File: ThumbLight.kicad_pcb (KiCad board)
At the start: 2 copper layers, 33 x 49 mm, 12 parts, among them J1 USB_A, SW1 RESET, SW2 A, SW3 B, SW4 MODE, U1 DHT11, U2 UA78M33_TO252, U3 ESP-12E, U4 TTL

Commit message: v1.1-beta improvements
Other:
- board text added: "TODO: - Regulator needs more space - Neopixel needs more space and flat underground"
- board text added: "v1.1-beta"
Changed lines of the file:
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@@
     (pad_to_mask_clearance 0)
     (pcbplotparams
-      (layerselection 0x0001000_fffffffe)
+      (layerselection 0x0000000_fffffffe)
       (disableapertmacros false)
       (usegerberextensions false)
@@
       (hpglpendiameter 15.000000)
       (dxfpolygonmode true)
-      (dxfimperialunits true)
+      (dxfimperialunits false)
       (dxfusepcbnewfont true)
       (psnegative false)
@@
     (effects (font (size 1.5 1.5) (thickness 0.3)))
   )
+  (gr_text "v1.1-beta" (at 101 97 90) (layer "F.SilkS")
+    (effects (font (size 1.5 1.5) (thickness 0.3)))
+  )
+  (gr_text "TODO:\n\n- Regulator needs more space\n- Neopixel needs more space and flat underground\n" (at 95 51) (layer "F.Fab")
+    (effects (font (size 1.5 1.5) (thickness 0.3)) (justify left))
+  )
   (segment (start 84 116.971493) (end 84 113.075) (width 0.6) (layer "B.Cu") (net 1))

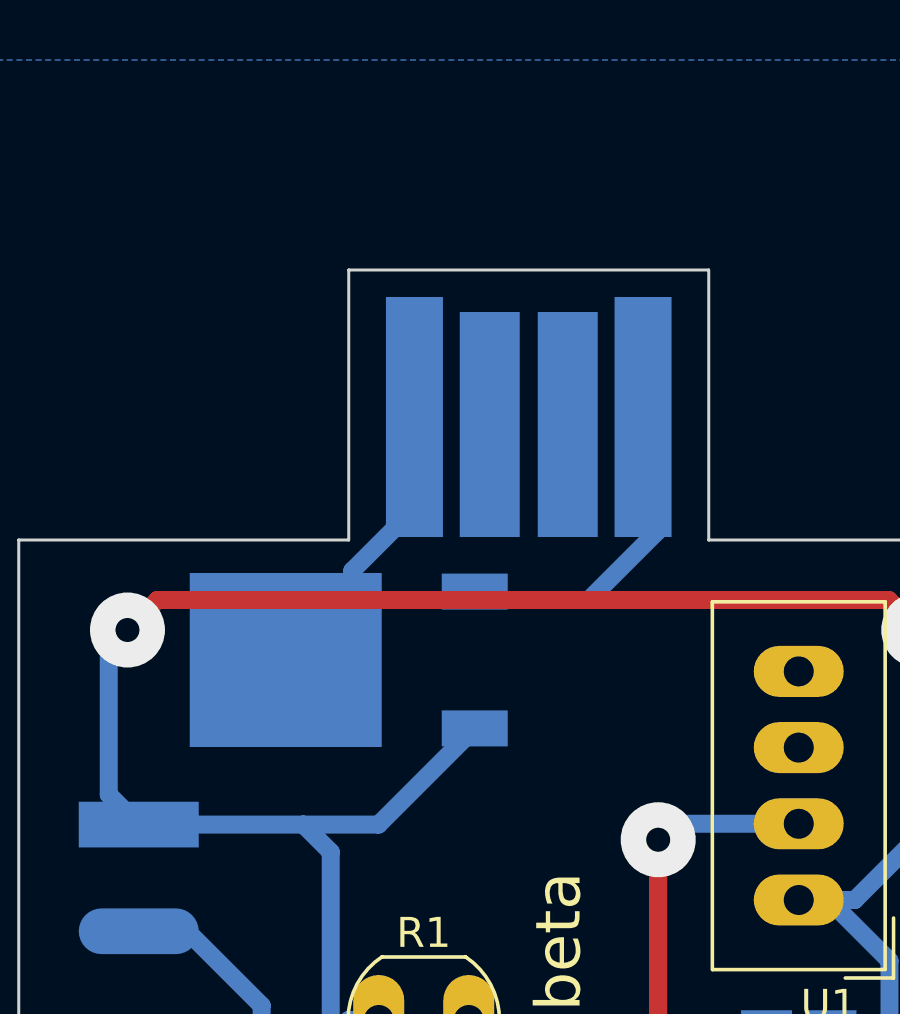
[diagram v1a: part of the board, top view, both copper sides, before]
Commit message: Elongate USB Plug
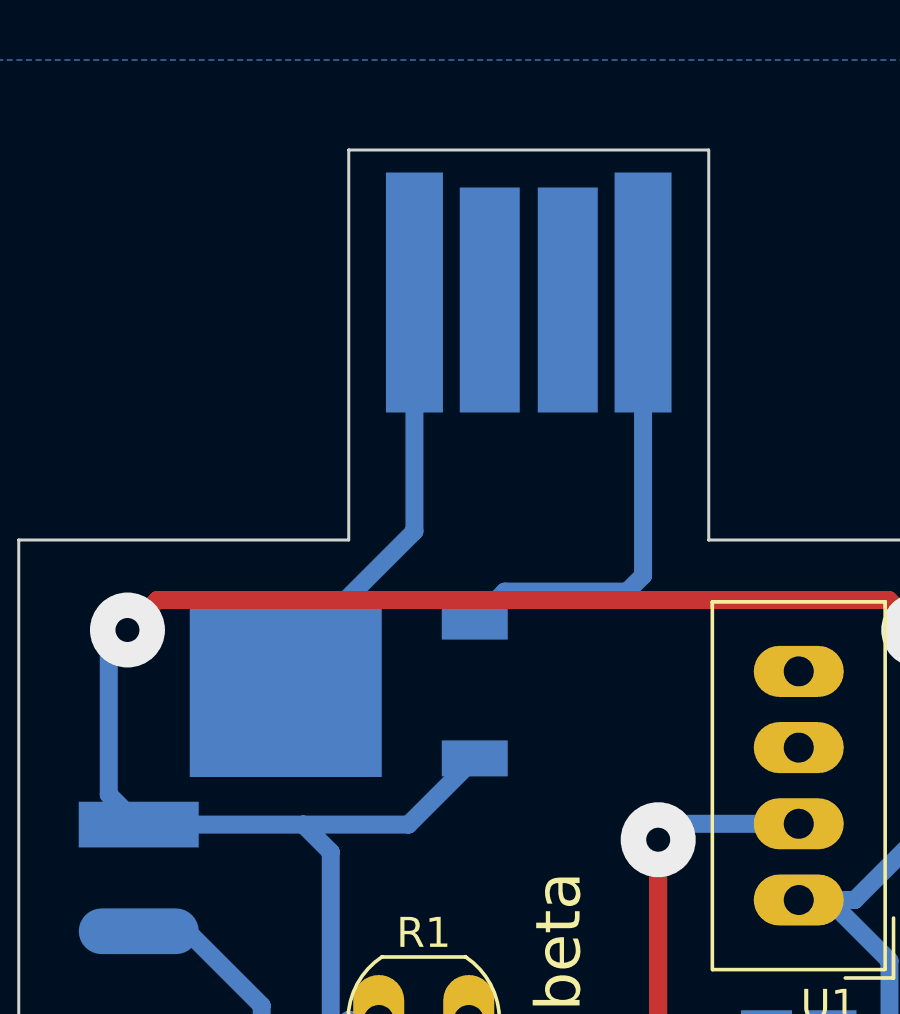
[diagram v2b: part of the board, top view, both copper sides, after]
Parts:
- moved J1 4.15 mm to (100.0, 67.8)
- moved U2 1.00 mm to (94.0, 86.0)
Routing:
- net GND: track 33.9 -> 39.1 mm
- net +5V: track 11.2 -> 15.7 mm
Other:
- board size 33 x 49 mm -> 33 x 53 mm
- board text added: "TODO: - Regulator needs more space - Neopixel needs more space and flat underground - Switches pads need to move to the outside of the switch"
- board text removed: "TODO: - Regulator needs more space - Neopixel needs more space and flat underground"
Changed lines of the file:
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@@
   )
   (footprint "usb-a-pcb:usb-a-pcb" (layer "B.Cu")
-    (at 100 72 180)
+    (at 100 67.85 180)
     (property "Sheetfile" "ThumbLight.kicad_sch")
     (property "Sheetname" "")
@@
       (polygon
         (pts
-          (xy 94 82)
-          (xy 106 82)
-          (xy 106 72)
-          (xy 94 72)
+          (xy 94 77.85)
+          (xy 106 77.85)
+          (xy 106 67.85)
+          (xy 94 67.85)
         )
       )
@@
   )
   (footprint "Package_TO_SOT_SMD:TO-252-2" (layer "B.Cu")
-    (at 94 85 180)
+    (at 94 86 180)
     (descr "TO-252 / DPAK SMD package, http://www.infineon.com/cms/en/product/packages/PG-TO252/PG-TO252-3-1/")
     (tags "DPAK TO-252 DPAK-3 TO-252-3 SOT-428")
@@
       (xy 83 81)
       (xy 94 81)
-      (xy 94 72)
-      (xy 106 72)
+      (xy 94 68)
+      (xy 106 68)
     ) (layer "Edge.Cuts") (width 0.1) (fill none))
   (gr_line (start 100 71) (end 100 129) (layer "F.Fab") (width 0.1))
@@
     (effects (font (size 1.5 1.5) (thickness 0.3)))
   )
-  (gr_text "TODO:\n\n- Regulator needs more space\n- Neopixel needs more space and flat underground\n" (at 95 51) (layer "F.Fab")
+  (gr_text "TODO:\n\n- Regulator needs more space\n- Neopixel needs more space and flat underground\n- Switches pads need to move to the outside of the switch" (at 95 51) (layer "F.Fab")
     (effects (font (size 1.5 1.5) (thickness 0.3)) (justify left))
   )
   (segment (start 84 116.971493) (end 84 113.075) (width 0.6) (layer "B.Cu") (net 1))
   (segment (start 84 108.925) (end 84 113.075) (width 0.6) (layer "B.Cu") (net 1))
+  (segment (start 91.9 85) (end 91.9 86) (width 0.6) (layer "B.Cu") (net 1))
   (segment (start 84.501497 117.47299) (end 84 116.971493) (width 0.6) (layer "B.Cu") (net 1))
-  (segment (start 94.12 82.02) (end 94.12 82.78) (width 0.6) (layer "B.Cu") (net 1))
-  (segment (start 94.12 82.78) (end 91.9 85) (width 0.6) (layer "B.Cu") (net 1))
   (segment (start 84 101.925) (end 84 113.075) (width 0.6) (layer "B.Cu") (net 1))
-  (segment (start 96.19 79.95) (end 94.12 82.02) (width 0.6) (layer "B.Cu") (net 1))
+  (segment (start 96.19 80.71) (end 91.9 85) (width 0.6) (layer "B.Cu") (net 1))
   (segment (start 88.651497 117.47299) (end 84.501497 117.47299) (width 0.6) (layer "B.Cu") (net 1))
-  (segment (start 96.19 76.9) (end 96.19 79.95) (width 0.6) (layer "B.Cu") (net 1))
+  (segment (start 96.19 72.75) (end 96.19 80.71) (width 0.6) (layer "B.Cu") (net 1))
   (segment (start 113 84) (end 112 83) (width 0.6) (layer "F.Cu") (net 2))
   (segment (start 87.624255 83) (end 86.624255 84) (width 0.6) (layer "F.Cu") (net 2))
@@
   (segment (start 112.025 112.022535) (end 112.317294 112.314829) (width 0.6) (layer "B.Cu") (net 2))
   (segment (start 93.399501 91.399501) (end 92.48618 90.48618) (width 0.6) (layer "B.Cu") (net 2))
+  (segment (start 95.99382 90.48618) (end 98.2 88.28) (width 0.6) (layer "B.Cu") (net 2))
   (segment (start 96 114.100499) (end 94.600499 115.5) (width 0.6) (layer "B.Cu") (net 2))
   (segment (start 112.025 95.025) (end 112.025 112.022535) (width 0.6) (layer "B.Cu") (net 2))
   (segment (start 86 84.624255) (end 86.624255 84) (width 0.6) (layer "B.Cu") (net 2))
-  (segment (start 94.99382 90.48618) (end 92.48618 90.48618) (width 0.6) (layer "B.Cu") (net 2))
+  (segment (start 92.48618 90.48618) (end 95.99382 90.48618) (width 0.6) (layer "B.Cu") (net 2))
   (segment (start 87 90.48618) (end 86 89.48618) (width 0.6) (layer "B.Cu") (net 2))
-  (segment (start 98.2 87.28) (end 94.99382 90.48618) (width 0.6) (layer "B.Cu") (net 2))
   (segment (start 93.399501 97.600499) (end 93.399501 91.399501) (width 0.6) (layer "B.Cu") (net 2))
   (segment (start 112.999999 90.867717) (end 113 84) (width 0.6) (layer "B.Cu") (net 2))
@@
   (segment (start 107.6 119.5) (end 109.25604 119.5) (width 0.6) (layer "B.Cu") (net 11))
   (segment (start 109.25604 119.5) (end 111.361211 117.394829) (width 0.6) (layer "B.Cu") (net 11))
-  (segment (start 104.3 80.7) (end 104.3 77.39) (width 0.6) (layer "B.Cu") (net 12))
-  (segment (start 98.48 83) (end 102 83) (width 0.6) (layer "B.Cu") (net 12))
-  (segment (start 104.3 77.39) (end 103.81 76.9) (width 0.6) (layer "B.Cu") (net 12))
-  (segment (start 98.2 82.72) (end 98.48 83) (width 0.6) (layer "B.Cu") (net 12))
-  (segment (start 102 83) (end 104.3 80.7) (width 0.6) (layer "B.Cu") (net 12))
+  (segment (start 103.28 82.72) (end 103.81 82.19) (width 0.6) (layer "B.Cu") (net 12))
+  (segment (start 103.81 82.19) (end 103.81 72.75) (width 0.6) (layer "B.Cu") (net 12))
+  (segment (start 99.2 82.72) (end 103.28 82.72) (width 0.6) (layer "B.Cu") (net 12))
+  (segment (start 98.2 83.72) (end 99.2 82.72) (width 0.6) (layer "B.Cu") (net 12))
   (segment (start 104.3495 99) (end 104.315267 98.965767) (width 0.6) (layer "F.Cu") (net 15))
   (segment (start 104.315267 98.965767) (end 104.315267 90.990811) (width 0.6) (layer "F.Cu") (net 15))
@@
   (segment (start 110.075 102.05) (end 110.075 97.925) (width 0.6) (layer "B.Cu") (net 17))
   (segment (start 110.2 110.56603) (end 110.2 102.935728) (width 0.6) (layer "B.Cu") (net 17))
+  (zone (net 0) (net_name "") (layers F&B.Cu) (hatch edge 0.508)
+    (connect_pads (clearance 0))
+    (min_thickness 0.254)
+    (keepout (tracks allowed) (vias allowed) (pads not_allowed) (copperpour not_allowed) (footprints allowed))
+    (fill (thermal_gap 0.508) (thermal_bridge_width 0.508))
+    (polygon
+      (pts
+        (xy 106 81)
+        (xy 93 81)
+        (xy 93 77)
+        (xy 106 77)
+      )
+    )
+  )
   (zone locked (net 1) (net_name "GND") (layer "B.Cu") (hatch edge 0.508)
     (connect_pads (clearance 0.2))

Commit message: Improvements over version 1.0
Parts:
- moved R2 1.07 mm to (97.0, 101.0)
- moved LIN1 0.96 mm to (87.0, 95.0)
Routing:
- net +3V3: track 112.7 -> 114.1 mm
- net Net-(U3-Pad2): track 26.8 -> 25.7 mm
- net +5V: track 15.7 -> 15.1 mm
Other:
- board text added: "Flash Problems: Detect >> 4MB Flash"
- board text added: "TODO: - Neopixel needs more space and flat underground - Switches pads need to move to the outside of the switch"
- board text removed: "TODO: - Regulator needs more space - Neopixel needs more space and flat underground - Switches pads need to move to the outside of the switch"
